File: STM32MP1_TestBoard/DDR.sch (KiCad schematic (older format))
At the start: 18 parts, among them U1 STM32MP157xAC, U2 MT41K256M16TW-107

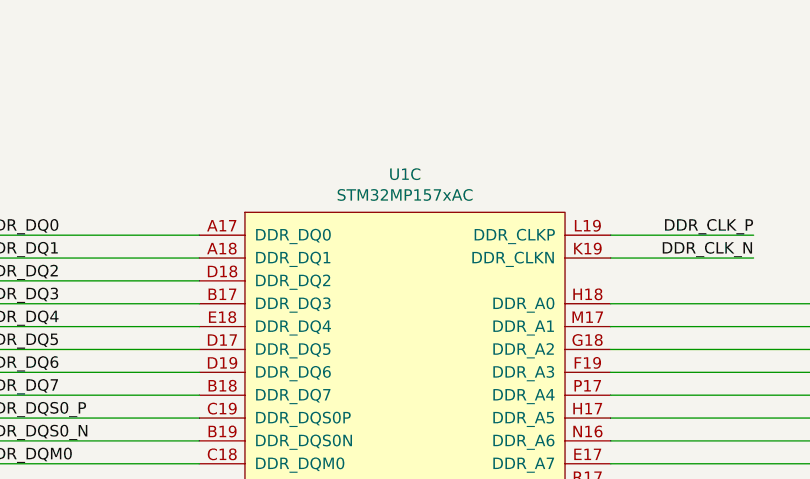
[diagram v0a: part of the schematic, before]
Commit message: corrected STM32MP157 footprint
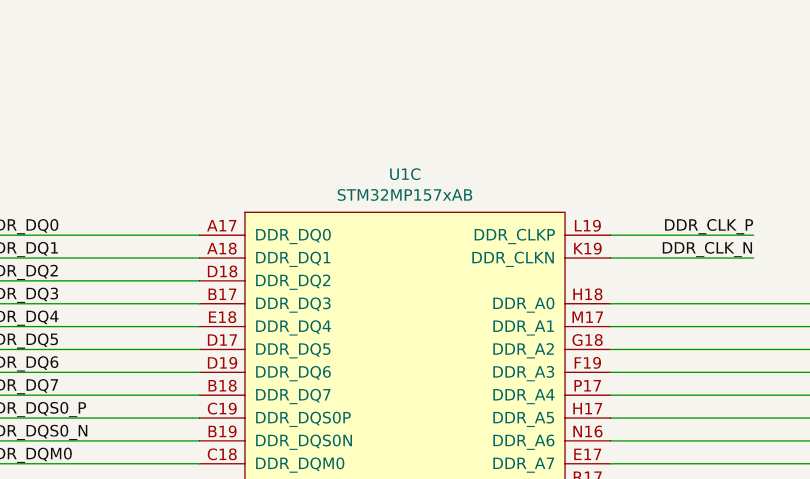
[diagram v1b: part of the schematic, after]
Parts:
- U1: value STM32MP157xAC -> STM32MP157xAB; footprint STM32MP151_LFBGA:BGA-361_19x19_16.0x16.0mm -> STM32MP151_LFBGA:BGA-354_19x19_16.0x16.0mm
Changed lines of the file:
@@
 P 3800 4125
 F 0 "U1" H 3800 5990 50  0000 C CNN
-F 1 "STM32MP157xAC" H 3800 5899 50  0000 C CNN
-F 2 "STM32MP151_LFBGA:BGA-361_19x19_16.0x16.0mm" H 3650 6025 50  0001 C CNN
+F 1 "STM32MP157xAB" H 3800 5899 50  0000 C CNN
+F 2 "STM32MP151_LFBGA:BGA-354_19x19_16.0x16.0mm" H 3650 6025 50  0001 C CNN
 F 3 "https://www.st.com/resource/en/datasheet/stm32mp151c.pdf" H 4450 4275 50  0001 C CNN
 F 4 "~" H 3800 4125 50  0001 C CNN "Mfr"
